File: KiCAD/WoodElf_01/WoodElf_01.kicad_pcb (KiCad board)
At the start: 2 copper layers, 95.2 x 100 mm, 114 parts, among them T1 BlankThrough-Hole, T10 BlankThrough-Hole, T11 BlankThrough-Hole, T12 BlankThrough-Hole, T13 BlankThrough-Hole, T2 BlankThrough-Hole, T3 BlankThrough-Hole, T4 BlankThrough-Hole, T5 BlankThrough-Hole, T6 BlankThrough-Hole, T7 BlankThrough-Hole, T8 BlankThrough-Hole, T9 BlankThrough-Hole

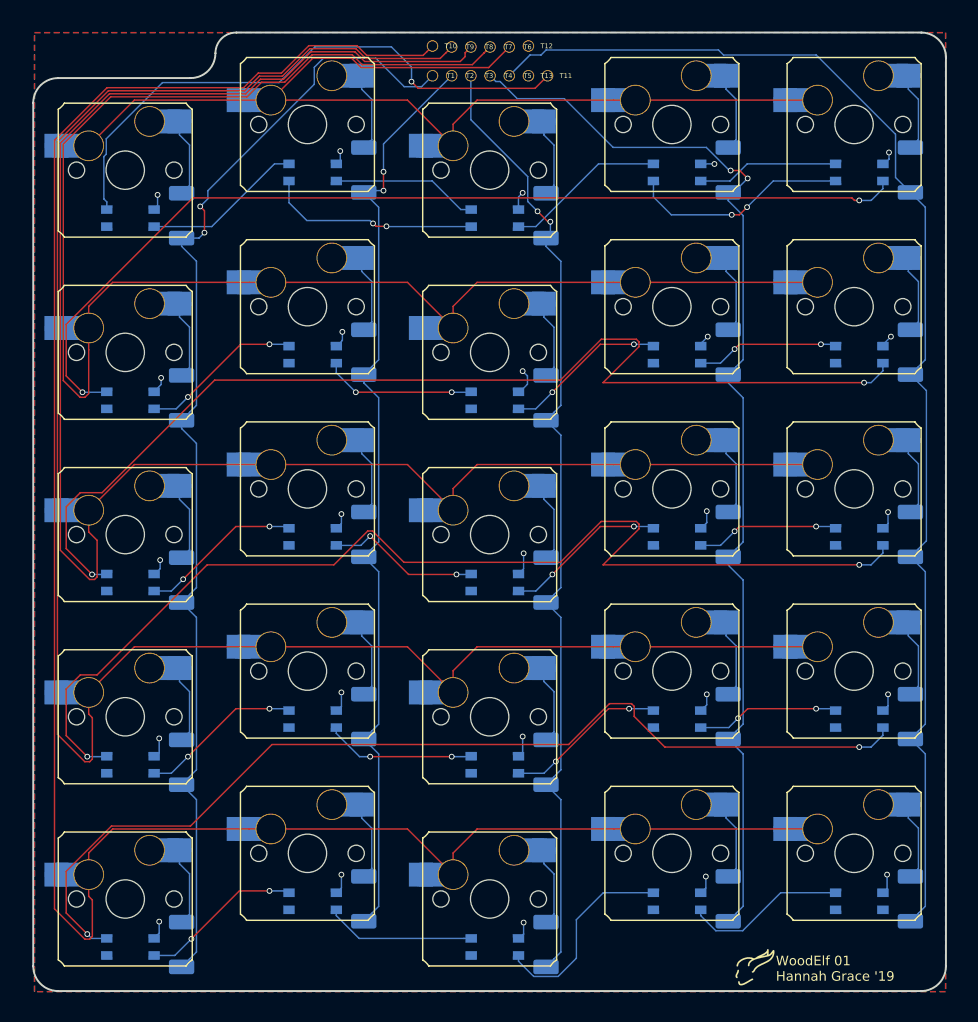
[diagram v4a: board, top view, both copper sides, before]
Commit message: fixed location of joystick pcb in folder
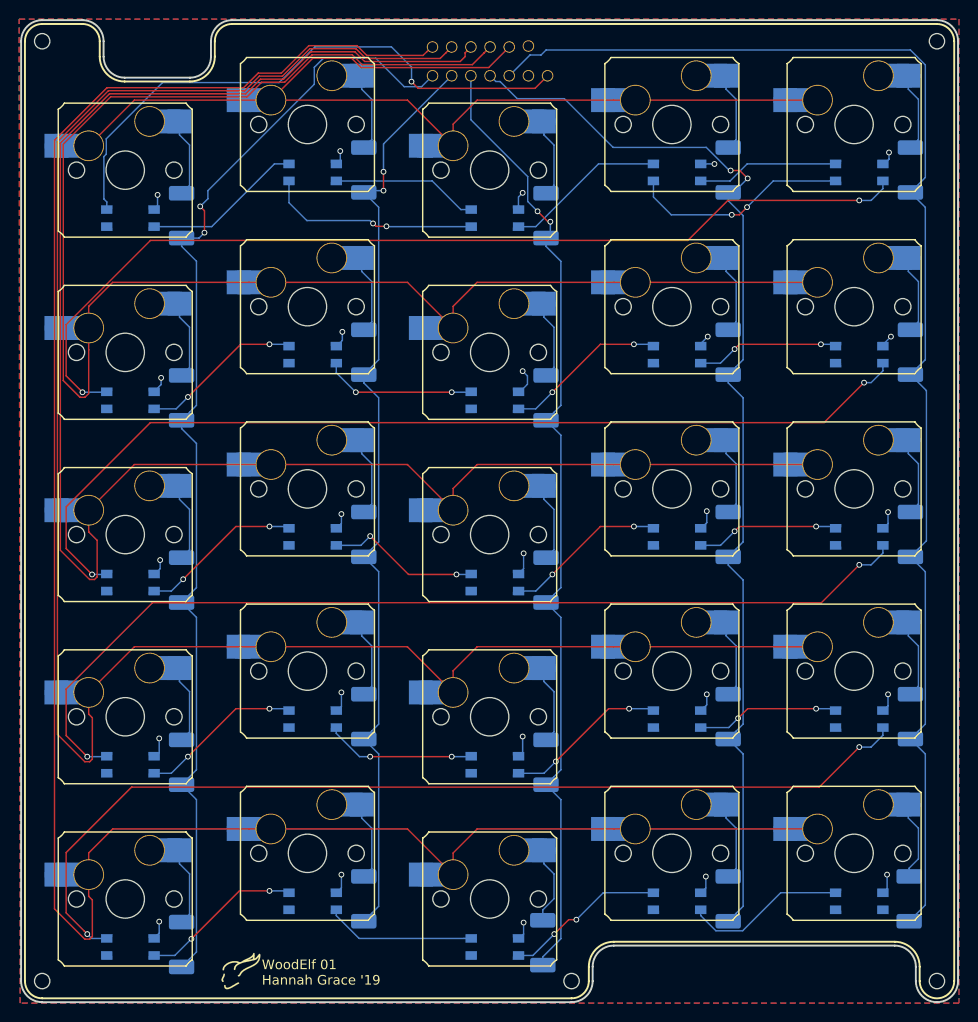
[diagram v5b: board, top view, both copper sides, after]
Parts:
- added G***: Tiefling_Logo, WoodElf_Lib:Tiefling_Logo, B.Cu at (135.0, 151.5)
- added Mount: Mount, WoodElf_Lib:Mount, F.Cu at (155.5, 152.4)
- added Mount: Mount, WoodElf_Lib:Mount, F.Cu at (193.6, 152.4)
- added Mount: Mount, WoodElf_Lib:Mount, F.Cu at (100.3, 152.4)
- added Mount: Mount, WoodElf_Lib:Mount, F.Cu at (100.3, 54.4)
- added Mount: Mount, WoodElf_Lib:Mount, F.Cu at (193.6, 54.4)
- moved G*** 53.6 mm to (121.0, 151.6)
- moved D23 0.38 mm to (152.5, 148.4)
- moved D25 0.13 mm to (190.7, 143.8)
- moved T10 0.10 mm to (141.0, 55.0)
- renumbered T1 to wT1
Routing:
- net /sheet5D51F414/Din: track 116.1 -> 101.9 mm
- net /sheet5D4DB164/Din: track 113.1 -> 101.6 mm
- net /Col5: track 133.0 -> 140.4 mm
- net /sheet5D53D8D4/Din: track 21.3 -> 16.8 mm, vias 0 -> 2
- net /sheet5D526D44/Din: track 105.9 -> 102.7 mm
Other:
- board size 95.2 x 100 mm -> 97.7 x 102.4 mm
- board text added: "Col1"
- board text added: "Col2"
- board text added: "Col3"
- board text added: "Col4"
- board text added: "Col5"
- board text added: "Din"
- board text added: "Row1"
- board text added: "Row2"
- board text added: "Row3"
- board text added: "Row4"
- board text added: "Row5"
- board text added: "VDD"
- board text added: "VSS"

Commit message: working out how to mount the joystick to the sandwich
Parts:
- added Mount: Mount, WoodElf_Lib:Mount, F.Cu at (120.1, 54.4)
- added Mount: Mount, WoodElf_Lib:Mount, F.Cu at (104.5, 54.4)
- moved T10 8.08 mm to (149.0, 56.1)
- moved T6 8.08 mm to (141.0, 56.1)
- moved T7 4.15 mm to (143.0, 56.1)
- moved T9 4.15 mm to (147.0, 56.1)
- moved T12 1.20 mm to (151.0, 56.1)
- moved T8 1.10 mm to (145.0, 56.1)
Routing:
- net /Row1: track 128.0 -> 118.8 mm
- net /Row5: track 237.8 -> 246.0 mm
- net /Row2: track 186.0 -> 181.3 mm
- net /Row4: track 220.0 -> 223.9 mm
- net /Row3: track 203.1 -> 202.5 mm
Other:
- board text added: "C1"
- board text added: "C2"
- board text added: "C3"
- board text added: "C4"
- board text added: "C5"
- board text added: "R1"
- board text added: "R2"
- board text added: "R3"
- board text added: "R4"
- board text added: "R5"
- board text removed: "Col1"
- board text removed: "Col2"
- board text removed: "Col3"
- board text removed: "Col4"
- board text removed: "Col5"
- board text removed: "Row1"
- board text removed: "Row2"
- board text removed: "Row3"
- board text removed: "Row4"
- board text removed: "Row5"

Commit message: completely redid everything
properly this time.
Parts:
- removed D21, D22, D23, D24, D25: DIODE, Diode_SMD:D_2010_5025Metric_Pad1.52x2.65mm_HandSolder
- removed the G*** at (135.0, 151.5)
- removed the G*** at (121.0, 151.6)
- removed H21, H22, H23, H24, H25: Kailh_HotSwap_SwitchMount, WoodElf_Lib:Kailh_HotSwap_Socket
- removed L21, L22, L23, L24, L25: SK6812MINI, WoodElf_Lib:LED_SK6812MINI_PLCC4_3.5x3.5mm_P1.75mm
- removed the Mount at (120.1, 54.4)
- removed the Mount at (104.5, 54.4)
- removed the Mount at (155.5, 152.4)
- removed the Mount at (193.6, 152.4)
- removed the Mount at (100.3, 152.4)
- removed the Mount at (100.3, 54.4)
- removed the Mount at (193.6, 54.4)
- removed S21, S22, S23, S24, S25: Kailh_RGB_Switch, WoodElf_Lib:SW_Cherry_MX1A_1.00u_PCB
- removed T11, wT1: BlankThrough-Hole, WoodElf_Lib:BlankThrough-Hole
- added D27: DIODE, WoodElf_Lib:D_SOD-123, B.Cu at (192.4, 125.3)
- added D28: DIODE, WoodElf_Lib:D_SOD-123, B.Cu at (192.4, 106.3)
- added D29: DIODE, WoodElf_Lib:D_SOD-123, B.Cu at (192.4, 87.2)
- added D30: DIODE, WoodElf_Lib:D_SOD-123, B.Cu at (192.4, 68.2)
- added G***: Tiefling_Logo, WoodElf_Lib:Tiefling_Logo, B.Cu at (186.3, 60.8)
- added G***: Tiefling_Logo, WoodElf_Lib:Tiefling_Logo, F.Cu at (172.0, 60.8)
- added H27: Kailh_HotSwap_SwitchMount, WoodElf_Lib:Kailh_HotSwap_Socket, F.Cu at (195.2, 134.5)
- added H28: Kailh_HotSwap_SwitchMount, WoodElf_Lib:Kailh_HotSwap_Socket, F.Cu at (195.2, 115.5)
- added H29: Kailh_HotSwap_SwitchMount, WoodElf_Lib:Kailh_HotSwap_Socket, F.Cu at (195.2, 96.4)
- added H30: Kailh_HotSwap_SwitchMount, WoodElf_Lib:Kailh_HotSwap_Socket, F.Cu at (195.2, 77.4)
- added L27: SK6812MINI, WoodElf_Lib:LED_SK6812MINI_PLCC4_3.5x3.5mm_P1.75mm, F.Cu at (197.8, 125.2)
- added L28: SK6812MINI, WoodElf_Lib:LED_SK6812MINI_PLCC4_3.5x3.5mm_P1.75mm, F.Cu at (197.8, 106.2)
- added L29: SK6812MINI, WoodElf_Lib:LED_SK6812MINI_PLCC4_3.5x3.5mm_P1.75mm, F.Cu at (197.8, 87.1)
- added L30: SK6812MINI, WoodElf_Lib:LED_SK6812MINI_PLCC4_3.5x3.5mm_P1.75mm, F.Cu at (197.8, 68.1)
- added Mount: Mount, WoodElf_Lib:Mount, F.Cu at (94.3, 59.6)
- added Mount: Mount, WoodElf_Lib:Mount, F.Cu at (94.3, 137.7)
- added Mount: Mount, WoodElf_Lib:Mount, F.Cu at (205.9, 137.6)
- added Mount: Mount, WoodElf_Lib:Mount, F.Cu at (205.9, 59.6)
- added S27: Kailh_RGB_Switch, WoodElf_Lib:SW_Cherry_MX1A_1.00u_PCB, F.Cu at (195.2, 134.5)
- added S28: Kailh_RGB_Switch, WoodElf_Lib:SW_Cherry_MX1A_1.00u_PCB, F.Cu at (195.2, 115.5)
- added S29: Kailh_RGB_Switch, WoodElf_Lib:SW_Cherry_MX1A_1.00u_PCB, F.Cu at (195.2, 96.4)
- added S30: Kailh_RGB_Switch, WoodElf_Lib:SW_Cherry_MX1A_1.00u_PCB, F.Cu at (195.2, 77.4)
- added T1: BlankThrough-Hole, WoodElf_Lib:BlankThrough-Hole, F.Cu at (193.2, 63.2)
- added T14: BlankThrough-Hole, WoodElf_Lib:BlankThrough-Hole, F.Cu at (203.2, 61.2)
- D1, D10, D11, D12, D13, D14, D15, D16, D17, D18, D19, D2, D20, D3, D4, D5, D6, D7, D8, D9: footprint Diode_SMD:D_2010_5025Metric_Pad1.52x2.65mm_HandSolder -> WoodElf_Lib:D_SOD-123
- moved T6 62.7 mm to (203.2, 63.2)
- moved T7 56.5 mm to (199.2, 61.2)
- moved T13 54.5 mm to (205.2, 63.2)
- moved T8 52.6 mm to (197.3, 61.2)
- moved T2 52.5 mm to (195.2, 63.2)
- moved T3 52.5 mm to (197.2, 63.2)
- moved T4 52.5 mm to (199.2, 63.2)
- moved T5 52.5 mm to (201.2, 63.2)
- moved T12 50.5 mm to (201.2, 61.2)
- moved T9 48.5 mm to (195.2, 61.2)
- moved T10 44.5 mm to (193.2, 61.2)
- moved H16 22.6 mm to (176.2, 134.5), turned to 180 degrees
- moved S16 22.6 mm to (176.2, 134.5), turned to 180 degrees
- moved H15 22.5 mm to (176.2, 115.5), turned to 180 degrees
- moved S15 22.5 mm to (176.2, 115.5), turned to 180 degrees
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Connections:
- L15 pad 1: /sheet5D51F414/Din -> /sheet5D22F5C7/Din
- L16 pad 1: /sheet5D526D44/Din -> /sheet5D22F5C1/Din
- L5 pad 1: /sheet5D4D3834/Din -> /sheet5D22F5D3/Din
- L6 pad 1: /sheet5D4DB164/Din -> /sheet5D22F5CD/Din
- T10 pad 1: /Row5 -> /Row4
- T12 pad 1: VDD -> /Din
- T13 pad 1: VSS -> VDD
- T6 pad 1: /Row1 -> /Col6
- T7 pad 1: /Row2 -> /Row1
- T8 pad 1: /Row3 -> /Row2
- T9 pad 1: /Row4 -> /Row3
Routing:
- net /Row5: track 246.0 -> 0.00 mm
- net /sheet5D526D44/Din: track 102.7 -> 0.00 mm, vias 2 -> 0
- net /Col6: track 0.00 -> 74.2 mm, vias 0 -> 1
- net /Col5: track 140.4 -> 91.2 mm, vias 0 -> 1
- net VDD: track 47.7 -> 0.00 mm, vias 25 -> 0
- net /Col2: track 98.2 -> 144.8 mm, vias 2 -> 1
- net /Din: track 60.8 -> 106.5 mm
- net /Col1: track 120.5 -> 162.5 mm, vias 2 -> 1
- net /Row4: track 223.9 -> 193.2 mm
- net /Row1: track 118.8 -> 148.6 mm
- net /Row3: track 202.5 -> 177.5 mm
- net /Col3: track 101.8 -> 126.3 mm, vias 2 -> 1
- net /Row2: track 181.3 -> 161.0 mm
- net /sheet5D22F5C1/Din: track 0.00 -> 17.4 mm, vias 0 -> 2
- net /sheet5D22F5D3/Din: track 0.00 -> 17.4 mm, vias 0 -> 2
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- added copper zone on B.Cu, net VDD
- added copper zone on F.Cu, net VSS
- removed copper zone on F.Cu, net VDD
- removed copper zone on B.Cu, net VSS
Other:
- board size 97.7 x 102.4 mm -> 114.9 x 81.3 mm
- board text removed: "C1"
- board text removed: "C2"
- board text removed: "C3"
- board text removed: "C4"
- board text removed: "C5"
- board text removed: "Din"
- board text removed: "R1"
- board text removed: "R2"
- board text removed: "R3"
- board text removed: "R4"
- board text removed: "R5"
- board text removed: "VDD"
- board text removed: "VSS"
